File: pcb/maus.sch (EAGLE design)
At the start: 82 parts, among them IC1 AD712R, Q2 BSS123, Q3 BSL307SP, Q4 BSS123, T1 BC847, T2 BC847, U1 ESP32-S2-WROOM, U2 CH340C, U3 CP2102, U4 LP3965EMP-3.3, U5 LSM9DS1TR

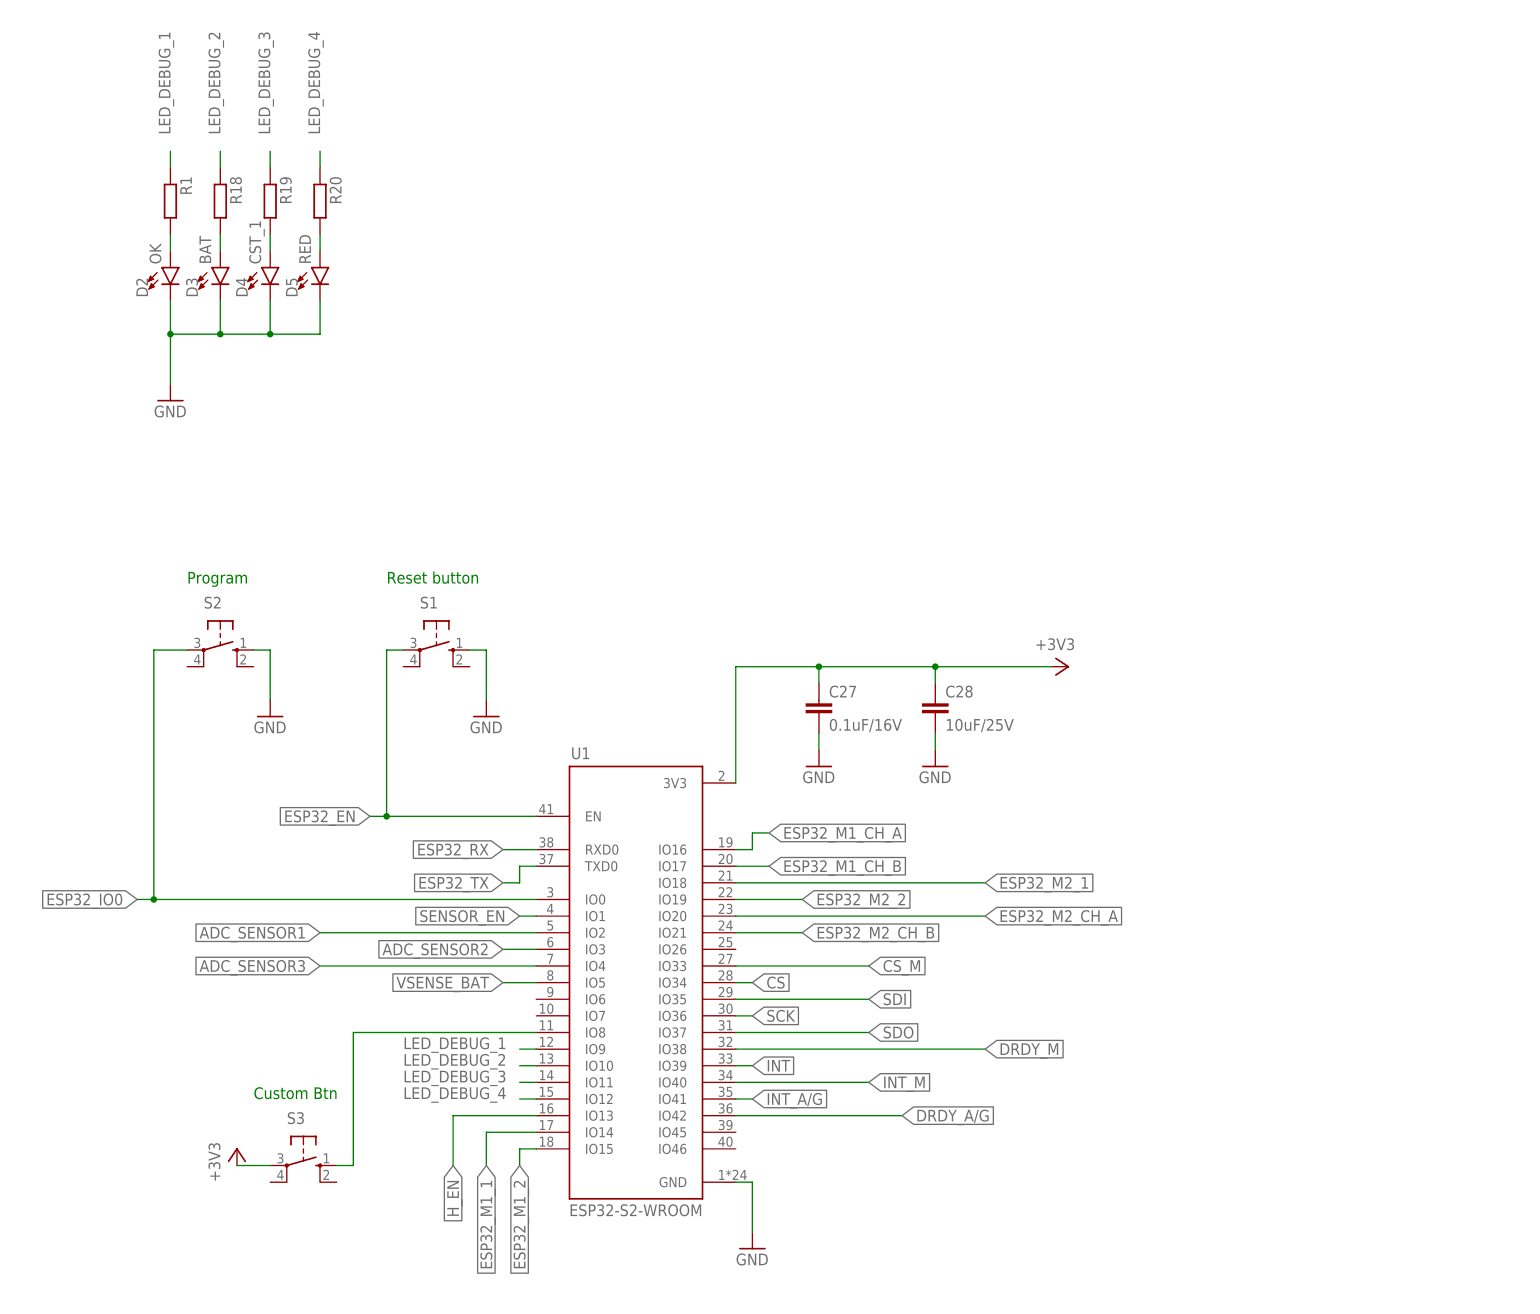
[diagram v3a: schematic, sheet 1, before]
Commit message: fix: added pullups on EN and IO0
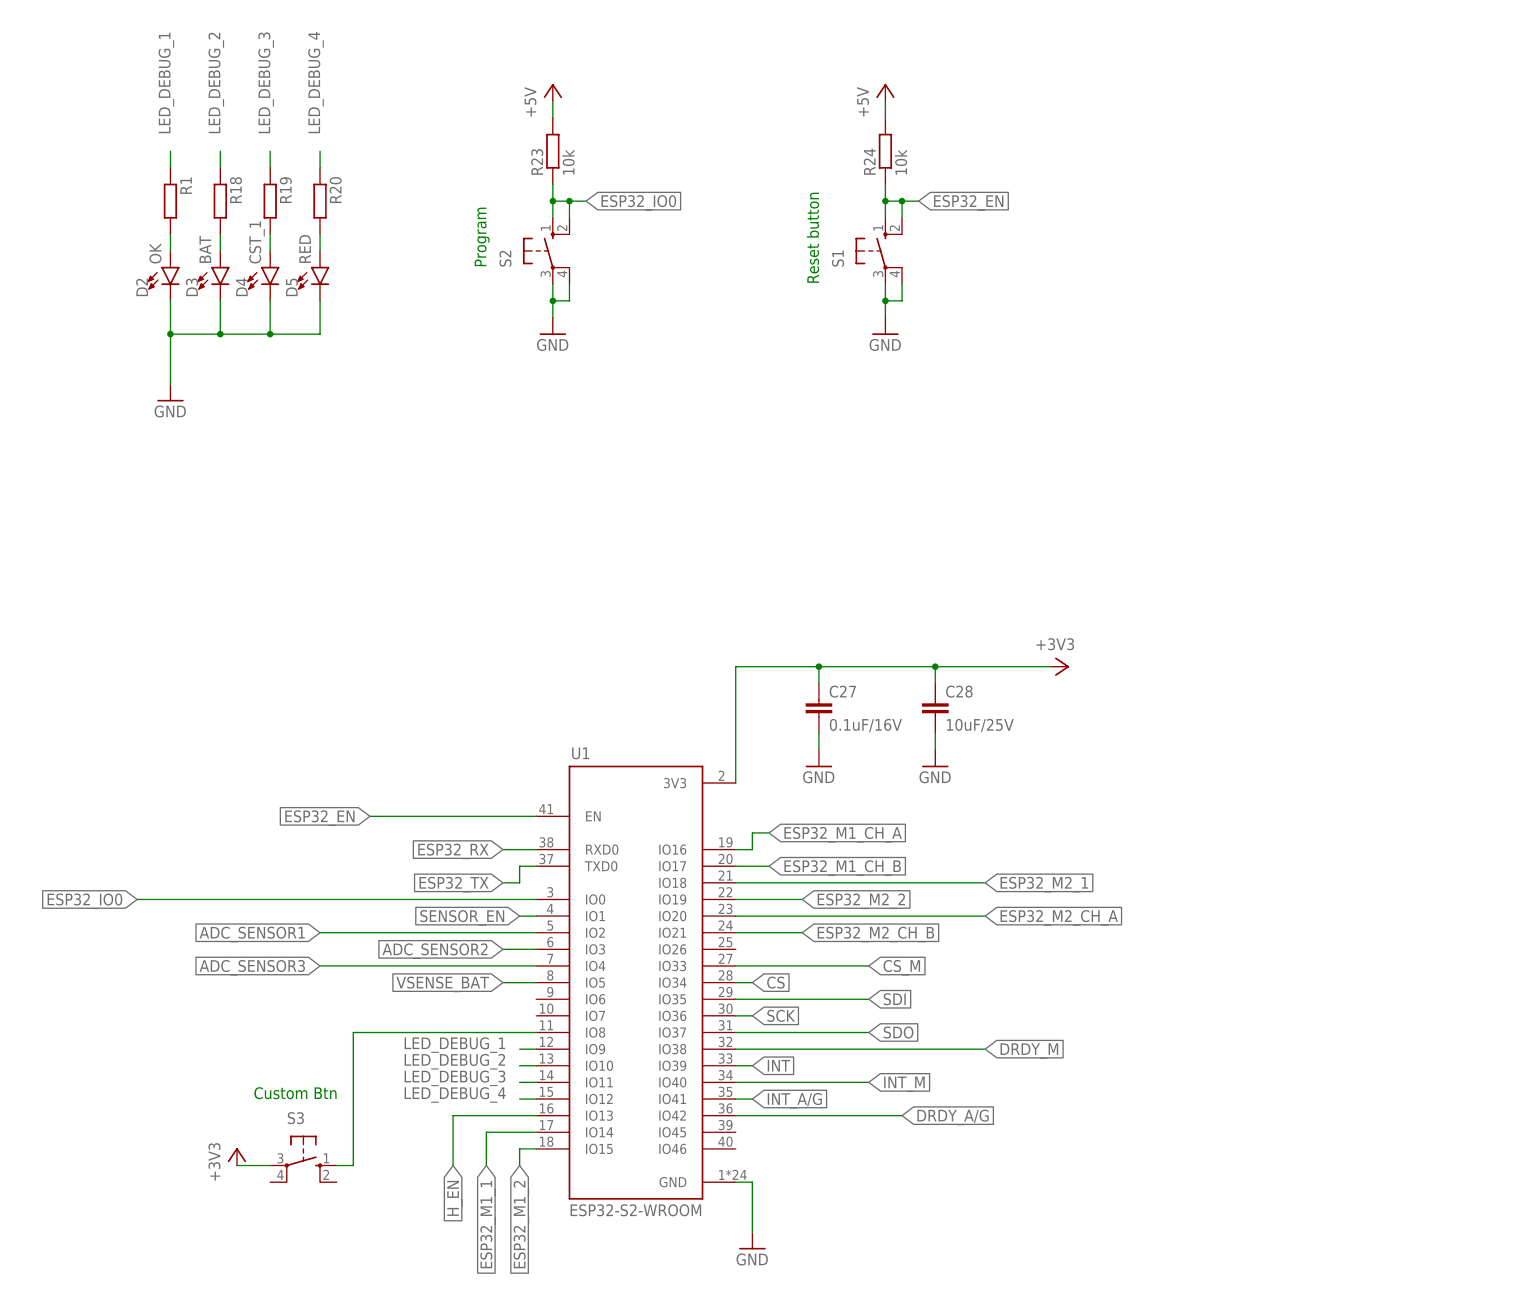
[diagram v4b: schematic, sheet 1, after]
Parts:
- added R23, R24: 10k, rcl:R-EU_R0805
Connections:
- net +5V: now also R23.2, R24.2
- net ESP32_EN: now also R24.1, S1.S, S1.S1; no longer S1.P
- net ESP32_IO0: now also R23.1, S2.S, S2.S1; no longer S2.P
- net GND: now also S1.P, S1.P1, S2.P, S2.P1; no longer S1.S, S2.S
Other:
- moved on the sheet: S1, S2
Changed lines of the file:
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@@
 <part name="Q4" library="transistor-small-signal" library_urn="urn:adsk.eagle:library:401" deviceset="BSS123" device="" package3d_urn="urn:adsk.eagle:package:28738/2"/>
 <part name="Q2" library="transistor-small-signal" library_urn="urn:adsk.eagle:library:401" deviceset="BSS123" device="" package3d_urn="urn:adsk.eagle:package:28738/2"/>
+<part name="R23" library="rcl" library_urn="urn:adsk.eagle:library:334" deviceset="R-EU_" device="R0805" package3d_urn="urn:adsk.eagle:package:23553/2" value="10k"/>
+<part name="R24" library="rcl" library_urn="urn:adsk.eagle:library:334" deviceset="R-EU_" device="R0805" package3d_urn="urn:adsk.eagle:package:23553/2" value="10k"/>
+<part name="P+8" library="supply1" library_urn="urn:adsk.eagle:library:371" deviceset="+5V" device=""/>
+<part name="P+9" library="supply1" library_urn="urn:adsk.eagle:library:371" deviceset="+5V" device=""/>
 </parts>
 <sheets>
 <sheet>
 <plain>
-<text x="63.5" y="124.46" size="1.778" layer="91">Reset button</text>
-<text x="33.02" y="124.46" size="1.778" layer="91">Program</text>
+<text x="129.54" y="170.18" size="1.778" layer="91" rot="R90">Reset button</text>
+<text x="78.74" y="172.72" size="1.778" layer="91" rot="R90">Program</text>
 <text x="43.18" y="45.72" size="1.778" layer="91">Custom Btn</text>
 </plain>
@@
 <attribute name="VALUE" x="116.84" y="20.32" size="1.778" layer="96"/>
 </instance>
-<instance part="S1" gate="1" x="71.12" y="114.3" smashed="yes" rot="R270">
-<attribute name="NAME" x="68.58" y="120.65" size="1.778" layer="95"/>
-<attribute name="VALUE" x="74.295" y="118.11" size="1.778" layer="96"/>
-</instance>
-<instance part="GND24" gate="1" x="78.74" y="104.14" smashed="yes">
-<attribute name="VALUE" x="76.2" y="101.6" size="1.778" layer="96"/>
-</instance>
-<instance part="S2" gate="1" x="38.1" y="114.3" smashed="yes" rot="R270">
-<attribute name="NAME" x="35.56" y="120.65" size="1.778" layer="95"/>
-<attribute name="VALUE" x="41.275" y="118.11" size="1.778" layer="96"/>
-</instance>
-<instance part="GND25" gate="1" x="45.72" y="104.14" smashed="yes">
-<attribute name="VALUE" x="43.18" y="101.6" size="1.778" layer="96"/>
+<instance part="S1" gate="1" x="139.7" y="175.26" smashed="yes">
+<attribute name="NAME" x="133.35" y="172.72" size="1.778" layer="95" rot="R90"/>
+<attribute name="VALUE" x="135.89" y="178.435" size="1.778" layer="96" rot="R90"/>
+</instance>
+<instance part="GND24" gate="1" x="139.7" y="162.56" smashed="yes">
+<attribute name="VALUE" x="137.16" y="160.02" size="1.778" layer="96"/>
+</instance>
+<instance part="S2" gate="1" x="88.9" y="175.26" smashed="yes">
+<attribute name="NAME" x="82.55" y="172.72" size="1.778" layer="95" rot="R90"/>
+<attribute name="VALUE" x="85.09" y="178.435" size="1.778" layer="96" rot="R90"/>
+</instance>
+<instance part="GND25" gate="1" x="88.9" y="162.56" smashed="yes">
+<attribute name="VALUE" x="86.36" y="160.02" size="1.778" layer="96"/>
 </instance>
 <instance part="S3" gate="1" x="50.8" y="35.56" smashed="yes" rot="R270">
@@
 <instance part="GND37" gate="1" x="147.32" y="96.52" smashed="yes">
 <attribute name="VALUE" x="144.78" y="93.98" size="1.778" layer="96"/>
+</instance>
+<instance part="R23" gate="G$1" x="88.9" y="190.5" smashed="yes" rot="R90">
+<attribute name="NAME" x="87.4014" y="186.69" size="1.778" layer="95" rot="R90"/>
+<attribute name="VALUE" x="92.202" y="186.69" size="1.778" layer="96" rot="R90"/>
+</instance>
+<instance part="R24" gate="G$1" x="139.7" y="190.5" smashed="yes" rot="R90">
+<attribute name="NAME" x="138.2014" y="186.69" size="1.778" layer="95" rot="R90"/>
+<attribute name="VALUE" x="143.002" y="186.69" size="1.778" layer="96" rot="R90"/>
+</instance>
+<instance part="P+8" gate="1" x="88.9" y="200.66" smashed="yes">
+<attribute name="VALUE" x="86.36" y="195.58" size="1.778" layer="96" rot="R90"/>
+</instance>
+<instance part="P+9" gate="1" x="139.7" y="200.66" smashed="yes">
+<attribute name="VALUE" x="137.16" y="195.58" size="1.778" layer="96" rot="R90"/>
 </instance>
 </instances>
@@
 <wire x1="119.38" y1="33.02" x2="119.38" y2="25.4" width="0.1524" layer="91"/>
 <pinref part="GND23" gate="1" pin="GND"/>
-</segment>
-<segment>
-<pinref part="S1" gate="1" pin="S"/>
-<wire x1="76.2" y1="114.3" x2="78.74" y2="114.3" width="0.1524" layer="91"/>
-<pinref part="GND24" gate="1" pin="GND"/>
-<wire x1="78.74" y1="114.3" x2="78.74" y2="106.68" width="0.1524" layer="91"/>
-</segment>
-<segment>
-<pinref part="S2" gate="1" pin="S"/>
-<wire x1="43.18" y1="114.3" x2="45.72" y2="114.3" width="0.1524" layer="91"/>
-<pinref part="GND25" gate="1" pin="GND"/>
-<wire x1="45.72" y1="114.3" x2="45.72" y2="106.68" width="0.1524" layer="91"/>
 </segment>
 <segment>
@@
 <wire x1="147.32" y1="99.06" x2="147.32" y2="101.6" width="0.1524" layer="91"/>
 </segment>
+<segment>
+<pinref part="S2" gate="1" pin="P"/>
+<pinref part="GND25" gate="1" pin="GND"/>
+<wire x1="88.9" y1="170.18" x2="88.9" y2="167.64" width="0.1524" layer="91"/>
+<pinref part="S2" gate="1" pin="P1"/>
+<wire x1="88.9" y1="167.64" x2="88.9" y2="165.1" width="0.1524" layer="91"/>
+<wire x1="91.44" y1="170.18" x2="91.44" y2="167.64" width="0.1524" layer="91"/>
+<wire x1="91.44" y1="167.64" x2="88.9" y2="167.64" width="0.1524" layer="91"/>
+<junction x="88.9" y="167.64"/>
+</segment>
+<segment>
+<pinref part="S1" gate="1" pin="P"/>
+<pinref part="GND24" gate="1" pin="GND"/>
+<wire x1="139.7" y1="170.18" x2="139.7" y2="167.64" width="0.1524" layer="91"/>
+<pinref part="S1" gate="1" pin="P1"/>
+<wire x1="139.7" y1="167.64" x2="139.7" y2="165.1" width="0.1524" layer="91"/>
+<wire x1="142.24" y1="170.18" x2="142.24" y2="167.64" width="0.1524" layer="91"/>
+<wire x1="142.24" y1="167.64" x2="139.7" y2="167.64" width="0.1524" layer="91"/>
+<junction x="139.7" y="167.64"/>
+</segment>
 </net>
 <net name="ESP32_EN" class="0">
 <segment>
 <pinref part="U1" gate="G$1" pin="EN"/>
-<wire x1="86.36" y1="88.9" x2="63.5" y2="88.9" width="0.1524" layer="91"/>
+<wire x1="86.36" y1="88.9" x2="60.96" y2="88.9" width="0.1524" layer="91"/>
 <label x="60.96" y="88.9" size="1.778" layer="95" rot="R180" xref="yes"/>
-<pinref part="S1" gate="1" pin="P"/>
-<wire x1="63.5" y1="88.9" x2="60.96" y2="88.9" width="0.1524" layer="91"/>
-<wire x1="66.04" y1="114.3" x2="63.5" y2="114.3" width="0.1524" layer="91"/>
-<wire x1="63.5" y1="114.3" x2="63.5" y2="88.9" width="0.1524" layer="91"/>
-<junction x="63.5" y="88.9"/>
+</segment>
+<segment>
+<pinref part="R24" gate="G$1" pin="1"/>
+<pinref part="S1" gate="1" pin="S"/>
+<wire x1="139.7" y1="185.42" x2="139.7" y2="182.88" width="0.1524" layer="91"/>
+<pinref part="S1" gate="1" pin="S1"/>
+<wire x1="139.7" y1="182.88" x2="139.7" y2="180.34" width="0.1524" layer="91"/>
+<wire x1="139.7" y1="182.88" x2="142.24" y2="182.88" width="0.1524" layer="91"/>
+<wire x1="142.24" y1="182.88" x2="142.24" y2="180.34" width="0.1524" layer="91"/>
+<junction x="139.7" y="182.88"/>
+<wire x1="142.24" y1="182.88" x2="144.78" y2="182.88" width="0.1524" layer="91"/>
+<junction x="142.24" y="182.88"/>
+<label x="144.78" y="182.88" size="1.778" layer="95" xref="yes"/>
 </segment>
 </net>
@@
 <segment>
 <pinref part="U1" gate="G$1" pin="IO0"/>
-<wire x1="86.36" y1="76.2" x2="27.94" y2="76.2" width="0.1524" layer="91"/>
+<wire x1="86.36" y1="76.2" x2="25.4" y2="76.2" width="0.1524" layer="91"/>
 <label x="25.4" y="76.2" size="1.778" layer="95" rot="R180" xref="yes"/>
-<pinref part="S2" gate="1" pin="P"/>
-<wire x1="27.94" y1="76.2" x2="25.4" y2="76.2" width="0.1524" layer="91"/>
-<wire x1="33.02" y1="114.3" x2="27.94" y2="114.3" width="0.1524" layer="91"/>
-<wire x1="27.94" y1="114.3" x2="27.94" y2="76.2" width="0.1524" layer="91"/>
-<junction x="27.94" y="76.2"/>
+</segment>
+<segment>
+<pinref part="R23" gate="G$1" pin="1"/>
+<pinref part="S2" gate="1" pin="S"/>
+<wire x1="88.9" y1="185.42" x2="88.9" y2="182.88" width="0.1524" layer="91"/>
+<pinref part="S2" gate="1" pin="S1"/>
+<wire x1="88.9" y1="182.88" x2="88.9" y2="180.34" width="0.1524" layer="91"/>
+<wire x1="88.9" y1="182.88" x2="91.44" y2="182.88" width="0.1524" layer="91"/>
+<wire x1="91.44" y1="182.88" x2="91.44" y2="180.34" width="0.1524" layer="91"/>
+<junction x="88.9" y="182.88"/>
+<wire x1="91.44" y1="182.88" x2="93.98" y2="182.88" width="0.1524" layer="91"/>
+<junction x="91.44" y="182.88"/>
+<label x="93.98" y="182.88" size="1.778" layer="95" xref="yes"/>
 </segment>
 </net>
@@
 </segment>
 </net>
+<net name="+5V" class="0">
+<segment>
+<pinref part="P+9" gate="1" pin="+5V"/>
+<pinref part="R24" gate="G$1" pin="2"/>
+<wire x1="139.7" y1="198.12" x2="139.7" y2="195.58" width="0.1524" layer="91"/>
+</segment>
+<segment>
+<pinref part="P+8" gate="1" pin="+5V"/>
+<pinref part="R23" gate="G$1" pin="2"/>
+<wire x1="88.9" y1="198.12" x2="88.9" y2="195.58" width="0.1524" layer="91"/>
+</segment>
+</net>
